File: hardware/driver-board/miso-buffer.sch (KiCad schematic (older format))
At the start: 2 parts, among them U3 NC7SZ125

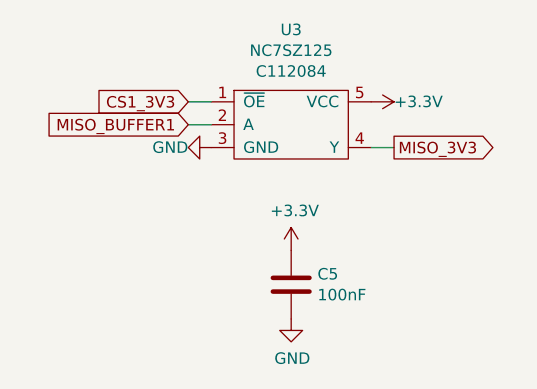
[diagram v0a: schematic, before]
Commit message: Rework power to four different voltage domains
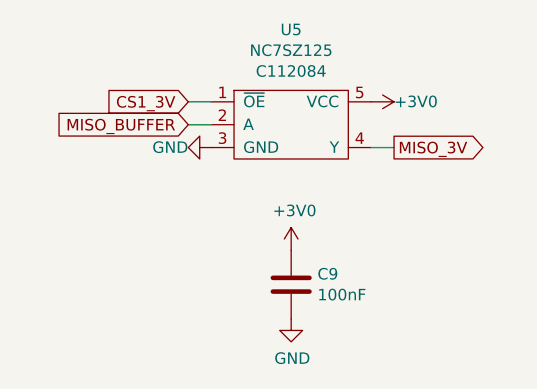
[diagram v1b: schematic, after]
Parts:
- renumbered C5 to C9, U3 to U5
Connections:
- net +3V3 renamed +3V0
- net CS1_3V3 renamed CS1_3V
- net MISO_3V3 renamed MISO_3V
- net MISO_BUFFER1 renamed MISO_BUFFER
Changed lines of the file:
@@
 $EndDescr
 $Comp
-L driver-board:NC7SZ125 U3
+L driver-board:NC7SZ125 U5
 U 1 1 5F016D73
 P 5900 3950
-F 0 "U3" H 5900 4365 50  0000 C CNN
+F 0 "U5" H 5900 4365 50  0000 C CNN
 F 1 "NC7SZ125" H 5900 4274 50  0000 C CNN
 F 2 "Package_TO_SOT_SMD:SOT-353_SC-70-5" H 5900 3900 50  0001 C CNN
@@
 $EndComp
 $Comp
-L power:+3.3V #PWR016
-U 1 1 5F017537
-P 6250 3850
-F 0 "#PWR016" H 6250 3700 50  0001 C CNN
-F 1 "+3.3V" V 6250 3950 50  0000 L CNN
-F 2 "" H 6250 3850 50  0001 C CNN
-F 3 "" H 6250 3850 50  0001 C CNN
-	1    6250 3850
-	0    1    1    0
-$EndComp
-$Comp
-L power:GND #PWR017
+L power:GND #PWR030
 U 1 1 5F017695
 P 5550 4050
-F 0 "#PWR017" H 5550 3800 50  0001 C CNN
+F 0 "#PWR030" H 5550 3800 50  0001 C CNN
 F 1 "GND" V 5550 3950 50  0000 R CNN
 F 2 "" H 5550 4050 50  0001 C CNN
@@
 $EndComp
 Text GLabel 6350 4050 2    50   Output ~ 0
-MISO_3V3
+MISO_3V
 Wire Wire Line
 	6250 4050 6350 4050
@@
 	5550 3850 5450 3850
 Text GLabel 5450 3850 0    50   Input ~ 0
-CS1_3V3
+CS1_3V
 Text GLabel 5450 3950 0    50   Input ~ 0
-MISO_BUFFER1
+MISO_BUFFER
 $Comp
-L Device:C C5
+L Device:C C9
 U 1 1 5F01887A
 P 5900 4650
-F 0 "C5" H 6015 4696 50  0000 L CNN
+F 0 "C9" H 6015 4696 50  0000 L CNN
 F 1 "100nF" H 6015 4605 50  0000 L CNN
 F 2 "Capacitor_SMD:C_0603_1608Metric" H 5938 4500 50  0001 C CNN
@@
 $EndComp
 $Comp
-L power:+3.3V #PWR018
-U 1 1 5F018F84
-P 5900 4500
-F 0 "#PWR018" H 5900 4350 50  0001 C CNN
-F 1 "+3.3V" H 5915 4673 50  0000 C CNN
-F 2 "" H 5900 4500 50  0001 C CNN
-F 3 "" H 5900 4500 50  0001 C CNN
-	1    5900 4500
-	1    0    0    -1
-$EndComp
-$Comp
-L power:GND #PWR019
+L power:GND #PWR032
 U 1 1 5F0190A9
 P 5900 4800
-F 0 "#PWR019" H 5900 4550 50  0001 C CNN
+F 0 "#PWR032" H 5900 4550 50  0001 C CNN
 F 1 "GND" H 5905 4627 50  0000 C CNN
 F 2 "" H 5900 4800 50  0001 C CNN
@@
 	1    0    0    -1
 $EndComp
+$Comp
+L power:+3V0 #PWR029
+U 1 1 5F04492E
+P 6250 3850
+F 0 "#PWR029" H 6250 3700 50  0001 C CNN
+F 1 "+3V0" V 6250 3950 50  0000 L CNN
+F 2 "" H 6250 3850 50  0001 C CNN
+F 3 "" H 6250 3850 50  0001 C CNN
+	1    6250 3850
+	0    1    1    0
+$EndComp
+$Comp
+L power:+3V0 #PWR031
+U 1 1 5F044AFF
+P 5900 4500
+F 0 "#PWR031" H 5900 4350 50  0001 C CNN
+F 1 "+3V0" H 5915 4673 50  0000 C CNN
+F 2 "" H 5900 4500 50  0001 C CNN
+F 3 "" H 5900 4500 50  0001 C CNN
+	1    5900 4500
+	1    0    0    -1
+$EndComp

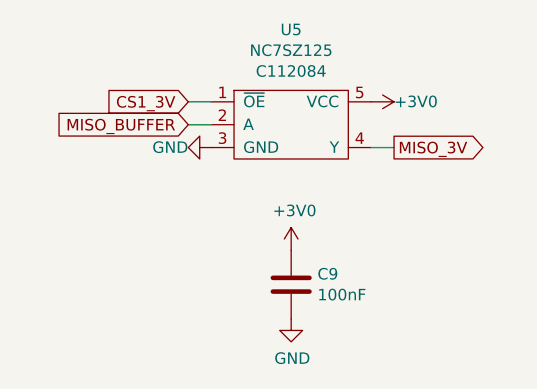
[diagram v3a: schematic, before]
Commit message: Adapt new SPI signal names from OSHWA
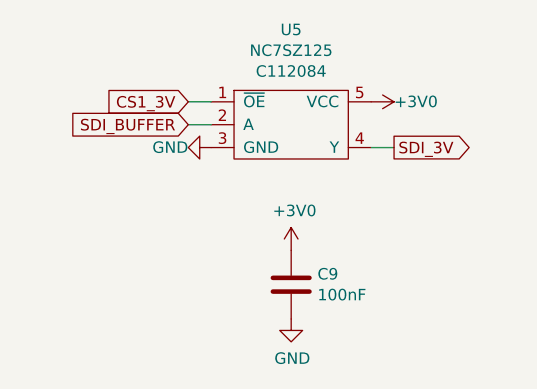
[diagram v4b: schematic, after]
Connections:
- net MISO_3V renamed SDI_3V
- net MISO_BUFFER renamed SDI_BUFFER
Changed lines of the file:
@@
 $EndComp
 Text GLabel 6350 4050 2    50   Output ~ 0
-MISO_3V
+SDI_3V
 Wire Wire Line
 	6250 4050 6350 4050
@@
 CS1_3V
 Text GLabel 5450 3950 0    50   Input ~ 0
-MISO_BUFFER
+SDI_BUFFER
 $Comp
 L Device:C C9

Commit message: Add missing JLCPCB part numbers
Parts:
- C9: JLCPCB (none) -> C14663
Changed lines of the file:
@@
 F 2 "Capacitor_SMD:C_0603_1608Metric" H 5938 4500 50  0001 C CNN
 F 3 "~" H 5900 4650 50  0001 C CNN
+F 4 "C14663" H 5900 4650 50  0001 C CNN "JLCPCB"
 	1    5900 4650
 	1    0    0    -1

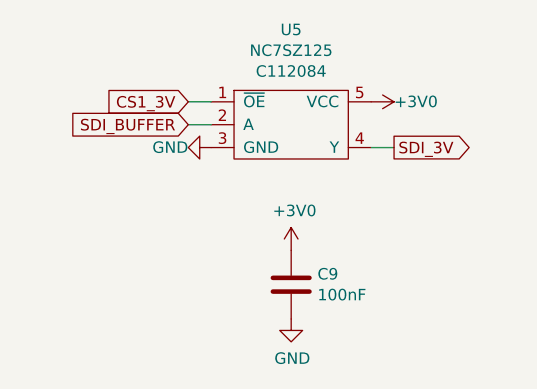
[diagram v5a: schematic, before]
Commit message: Rename JLCPCB to LCSC and update PCB
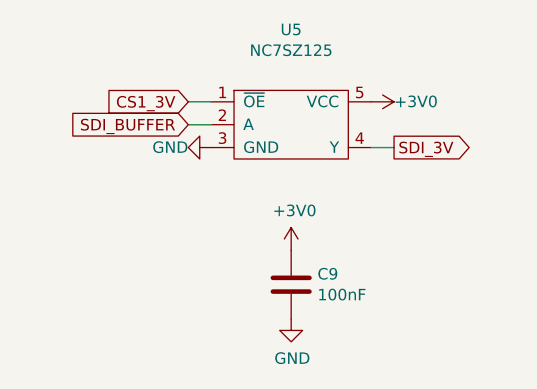
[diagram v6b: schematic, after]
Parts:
- C9: JLCPCB C14663 -> (none); LCSC (none) -> C14663
- U5: JLCPCB C112084 -> (none); LCSC (none) -> C112084
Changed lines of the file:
@@
 F 2 "Package_TO_SOT_SMD:SOT-353_SC-70-5" H 5900 3900 50  0001 C CNN
 F 3 "" H 5900 3900 50  0001 C CNN
-F 4 "C112084" H 5900 4183 50  0000 C CNN "JLCPCB"
+F 4 "C112084" H 5900 3950 50  0001 C CNN "LCSC"
 	1    5900 3950
 	1    0    0    -1
@@
 F 2 "Capacitor_SMD:C_0603_1608Metric" H 5938 4500 50  0001 C CNN
 F 3 "~" H 5900 4650 50  0001 C CNN
-F 4 "C14663" H 5900 4650 50  0001 C CNN "JLCPCB"
+F 4 "C14663" H 5900 4650 50  0001 C CNN "LCSC"
 	1    5900 4650
 	1    0    0    -1

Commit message: Add drop-in replacement for buffer IC
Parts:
- U5: footprint Package_TO_SOT_SMD:SOT-353_SC-70-5 -> Package_TO_SOT_SMD:SOT-23-5; LCSC C112084 -> C7420
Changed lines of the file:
@@
 F 0 "U5" H 5900 4365 50  0000 C CNN
 F 1 "NC7SZ125" H 5900 4274 50  0000 C CNN
-F 2 "Package_TO_SOT_SMD:SOT-353_SC-70-5" H 5900 3900 50  0001 C CNN
+F 2 "Package_TO_SOT_SMD:SOT-23-5" H 5900 3900 50  0001 C CNN
 F 3 "" H 5900 3900 50  0001 C CNN
-F 4 "C112084" H 5900 3950 50  0001 C CNN "LCSC"
+F 4 "C7420" H 5900 3950 50  0001 C CNN "LCSC"
 	1    5900 3950
 	1    0    0    -1
